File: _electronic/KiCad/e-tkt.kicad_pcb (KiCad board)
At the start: 2 copper layers, 71.1 x 63 mm, 82 parts, among them J2 USB4120-03-C_REVA, Q1 SS8050-G, Q2 SS8050-G, U2 AZ1117I-3.3, U6 ESP32-S3-WROOM-1-N8R2

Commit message: needs revision
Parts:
- removed D2: LED, LED_SMD:LED_0603_1608Metric_Pad1.05x0.95mm_HandSolder
- added D11: LED, LED_SMD:LED_0603_1608Metric_Pad1.05x0.95mm_HandSolder, F.Cu at (140.3, -204.7)
- added R2: 430R, Resistor_SMD:R_0603_1608Metric, F.Cu at (138.7, -207.3)
- added TP_IO15: TestPoint, TestPoint:TestPoint_Pad_D1.0mm, B.Cu at (151.4, -208.8)
- added TP_IO18: TestPoint, TestPoint:TestPoint_Pad_D1.0mm, B.Cu at (151.4, -206.8)
- added TP_IO5: TestPoint, TestPoint:TestPoint_Pad_D1.0mm, B.Cu at (151.4, -214.9)
- added TP_IO6: TestPoint, TestPoint:TestPoint_Pad_D1.0mm, B.Cu at (151.4, -212.9)
- added TP_IO7: TestPoint, TestPoint:TestPoint_Pad_D1.0mm, B.Cu at (151.4, -210.8)
- added TP_IO8: TestPoint, TestPoint:TestPoint_Pad_D1.0mm, B.Cu at (151.4, -204.7)
- moved C11 2.54 mm to (141.7, -207.3)
- moved C10 1.52 mm to (140.2, -207.3)
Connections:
- C11 pad 1: Net-(C11-Pad1) -> +3.3V
- U6 pad 11: unconnected-(U6-Pad11) -> Net-(U6-Pad11)
- U6 pad 12: unconnected-(U6-Pad12) -> Net-(U6-Pad12)
- U6 pad 5: unconnected-(U6-Pad5) -> Net-(U6-Pad5)
- U6 pad 6: unconnected-(U6-Pad6) -> Net-(U6-Pad6)
- U6 pad 7: unconnected-(U6-Pad7) -> Net-(U6-Pad7)
- U6 pad 8: unconnected-(U6-Pad8) -> Net-(U6-Pad8)
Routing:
- net +3.3V: track 266.6 -> 277.8 mm
- net Net-(U6-Pad8): track 0.00 -> 5.06 mm, vias 0 -> 1
- net GNDREF: track 419.0 -> 423.8 mm, vias 11 -> 10
- net Net-(U6-Pad7): track 0.00 -> 4.74 mm, vias 0 -> 1
- net Net-(U6-Pad12): track 0.00 -> 4.34 mm, vias 0 -> 1
- net Net-(U6-Pad11): track 0.00 -> 4.28 mm, vias 0 -> 1
- net Net-(U6-Pad6): track 0.00 -> 4.13 mm, vias 0 -> 1
- net Net-(U6-Pad5): track 0.00 -> 4.09 mm, vias 0 -> 1
- net IO20 D+: track 29.6 -> 31.7 mm
- net Net-(D11-Pad2): track 0.00 -> 2.04 mm
- net Net-(C11-Pad1): track 1.81 -> 0.00 mm
- net +12V: track 188.3 -> 190.1 mm
- net IO19 D-: track 36.0 -> 37.8 mm
- net Net-(J_masterpower1-Pad1): track 23.3 -> 24.9 mm
- net IO16: track 49.1 -> 50.3 mm
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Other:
- board text added: "05"
- board text added: "06"
- board text added: "07"
- board text added: "08"
- board text added: "15"
- board text added: "18"
- board text added: "GPIOs"

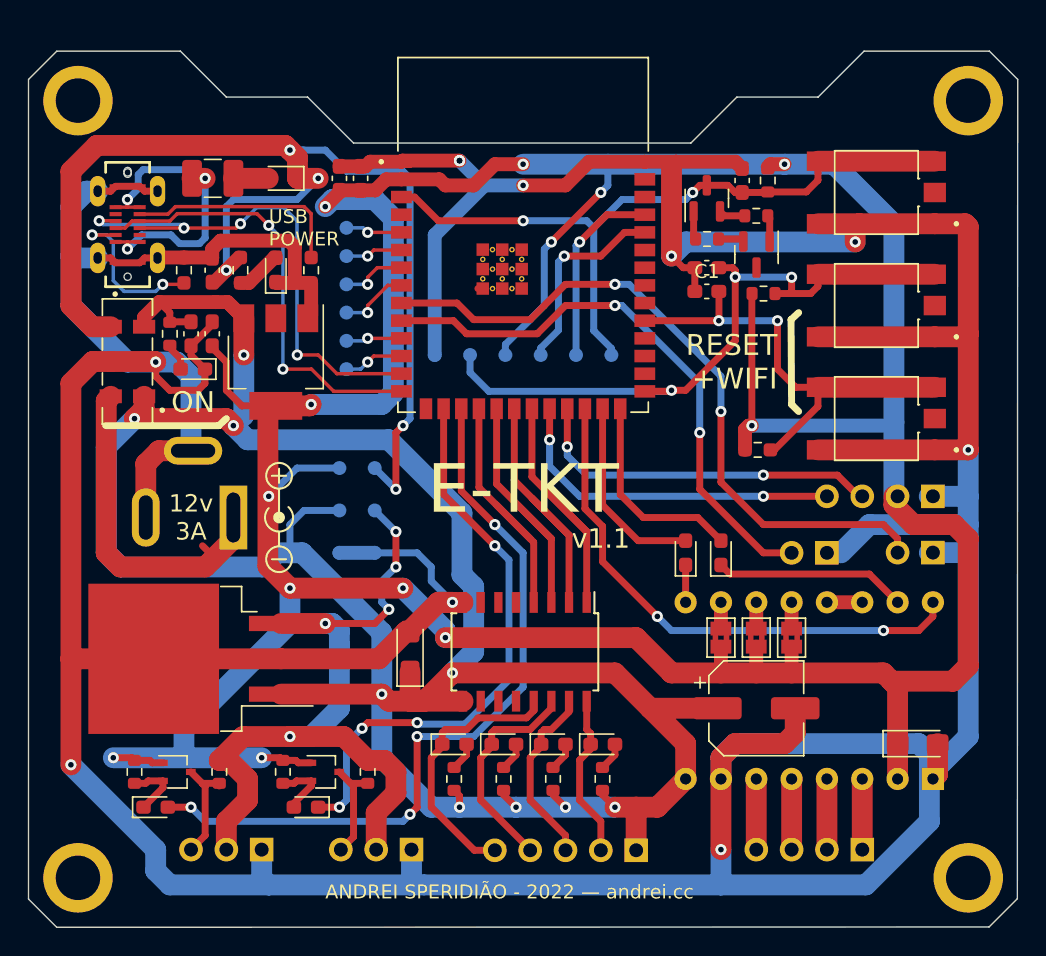
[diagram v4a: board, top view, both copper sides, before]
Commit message: tvs diode, ground plane, schematics layout
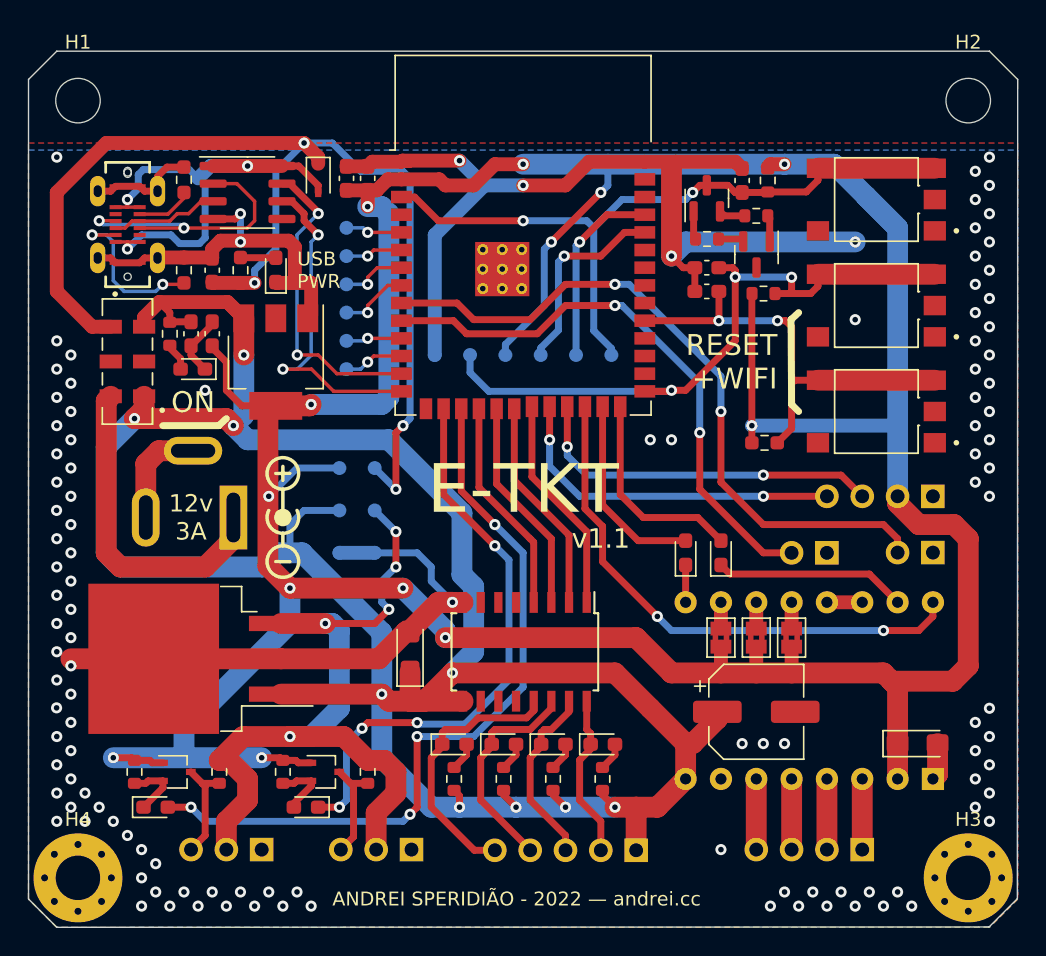
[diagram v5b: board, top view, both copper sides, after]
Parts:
- removed C13: 10uF/25v, Capacitor_SMD:C_0603_1608Metric_Pad1.08x0.95mm_HandSolder
- removed F2: 500mA, Fuse:Fuse_1210_3225Metric_Pad1.42x2.65mm_HandSolder
- removed REF**: Symbol_Barrel_Polarity, Symbol:Symbol_Barrel_Polarity
- removed REF** (x4): MountingHole_3.2mm_M3, MountingHole:MountingHole_3.2mm_M3
- removed REF**: OSHW-Symbol_6.7x6mm_SilkScreen, Symbol:OSHW-Symbol_6.7x6mm_SilkScreen
- added C2: 10uF/25v, Capacitor_SMD:C_0603_1608Metric_Pad1.08x0.95mm_HandSolder, F.Cu at (141.7, -211.8)
- added H1: MountingHole_Pad, MountingHole:MountingHole_3.2mm_M3, F.Cu at (132.1, -224.0)
- added H2: MountingHole_Pad, MountingHole:MountingHole_3.2mm_M3, F.Cu at (196.1, -224.0)
- added H3: MountingHole_Pad, MountingHole:MountingHole_3.2mm_M3_Pad_Via, F.Cu at (196.1, -168.1)
- added H4: MountingHole_Pad, MountingHole:MountingHole_3.2mm_M3_Pad_Via, F.Cu at (132.1, -168.1)
- added U1: USB6B1, Package_SO:SOIC-8_3.9x4.9mm_P1.27mm, F.Cu at (144.3, -217.4)
- U6: footprint SnapEDA Library:XCVR_ESP32-S3-WROOM-1-N16R2 -> RF_Module:ESP32-S3-WROOM-1
- U_6v2: footprint Package_TO_SOT_SMD:TO-263-3_TabPin2 -> Package_TO_SOT_SMD:TO-263-2
- moved R21 11.2 mm to (139.7, -218.3), turned to -90 degrees
- moved D3 2.54 mm to (149.4, -218.4), turned to -90 degrees
- moved R4 0.71 mm to (181.4, -199.4), turned to 180 degrees
- moved S_BOOT1 0.51 mm to (189.5, -216.9)
- moved C6 0.51 mm to (152.9, -218.4)
- moved C7 0.51 mm to (151.4, -218.4)
- moved S_WIFIRESET1 0.51 mm to (189.5, -201.7)
- moved C8 0.25 mm to (180.8, -180.1)
- turned R1 to 90 degrees
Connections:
- D3 pad 2: Net-(D3-Pad2) -> /VBUS_A
- J2 pad A4: Net-(F2-Pad1) -> /VBUS_A
- J2 pad A6: IO20 D+ -> /D1+
- J2 pad A7: IO19 D- -> /D1-
- J2 pad A9: Net-(F2-Pad1) -> /VBUS_A
- J2 pad B4: Net-(F2-Pad1) -> /VBUS_A
- J2 pad B6: IO20 D+ -> /D1+
- J2 pad B7: IO19 D- -> /D1-
- J2 pad B9: Net-(F2-Pad1) -> /VBUS_A
- R6 pad 1: +5V -> Net-(D_USBIN1-Pad2)
- R6 pad 2: Net-(D_USBIN1-Pad2) -> +5V
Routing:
- net GNDREF: track 423.8 -> 159.2 mm, vias 10 -> 117
- net /VBUS_A: track 0.00 -> 35.2 mm, vias 0 -> 3
- net Net-(F2-Pad1): track 23.5 -> 0.00 mm, vias 3 -> 0
- net /D1-: track 0.00 -> 20.9 mm, vias 0 -> 2
- net IO19 D-: track 37.8 -> 22.9 mm, vias 4 -> 2
- net Net-(J2-PadB5): track 15.9 -> 4.07 mm
- net /D1+: track 0.00 -> 7.81 mm
- net IO20 D+: track 31.7 -> 24.4 mm
- net +3.3V: track 277.8 -> 272.9 mm
- net IO13: track 19.3 -> 15.6 mm
- net IO12: track 19.3 -> 15.6 mm
- net IO11: track 19.3 -> 15.6 mm
- net IO10: track 19.0 -> 15.6 mm
- net +5V: track 84.0 -> 81.4 mm, vias 5 -> 4
- net Net-(D3-Pad2): track 2.51 -> 0.00 mm
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- added copper zone on B.Cu, net GNDREF
- added copper zone on F.Cu, net GNDREF
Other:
- outline, holes or cut-outs redrawn
- board text added: "USB PWR"
- board text removed: "USB POWER"

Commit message: fixed esp footprint/symbol, plus vias and holes
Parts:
- removed U6: ESP32-S3-WROOM-1-N8R2, RF_Module:ESP32-S3-WROOM-1
- added U3: ESP32-S3-WROOM-1-N8R2_Andrei, SnapEDA Library:ESP32-S3-WROOM-1_Andrei, F.Cu at (164.1, -214.4)
- H1, H2: footprint MountingHole:MountingHole_3.2mm_M3 -> MountingHole:MountingHole_3.2mm_M3_Pad_Via
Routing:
- net GNDREF: track 159.2 -> 82.4 mm, vias 117 -> 166
- net +5V: track 81.4 -> 62.6 mm, vias 4 -> 5
- net +3.3V: track 272.9 -> 274.5 mm

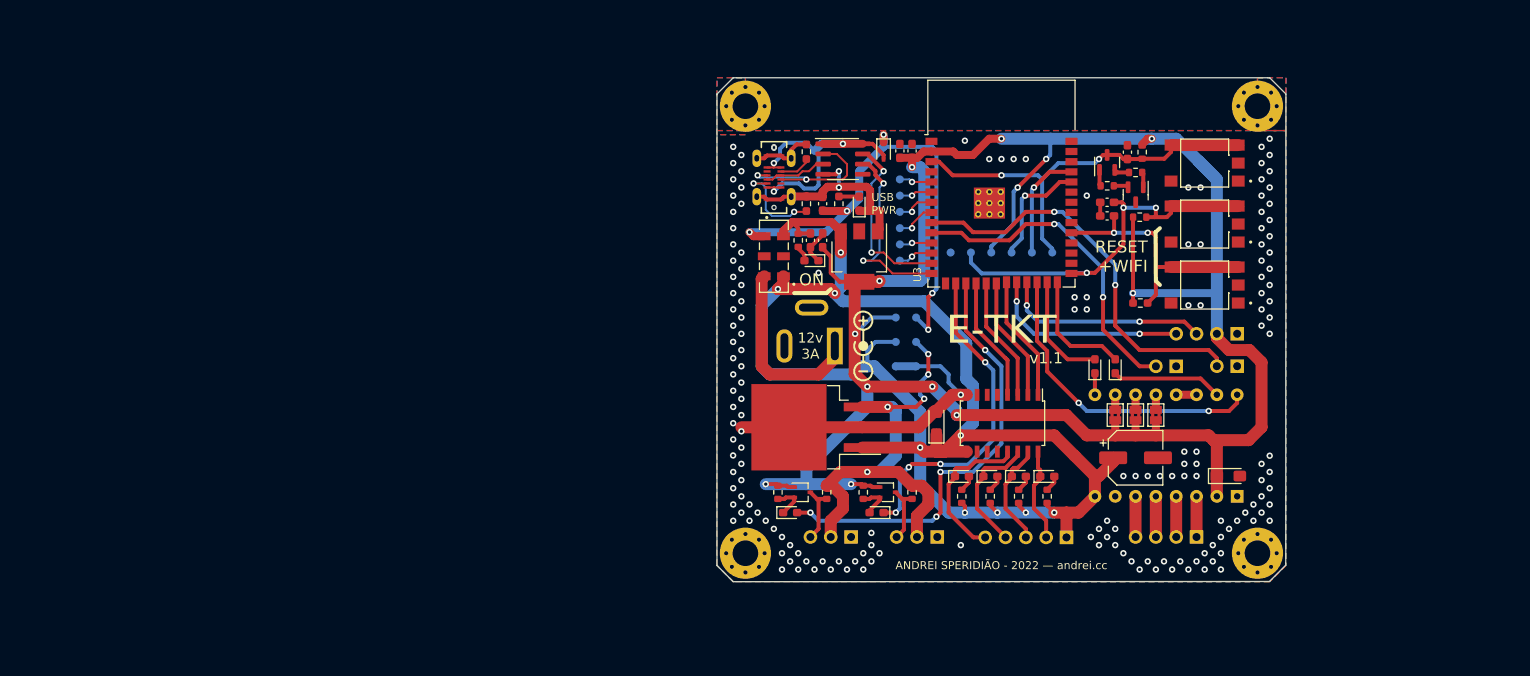
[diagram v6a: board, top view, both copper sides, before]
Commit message: bigger board, switch back to esp32
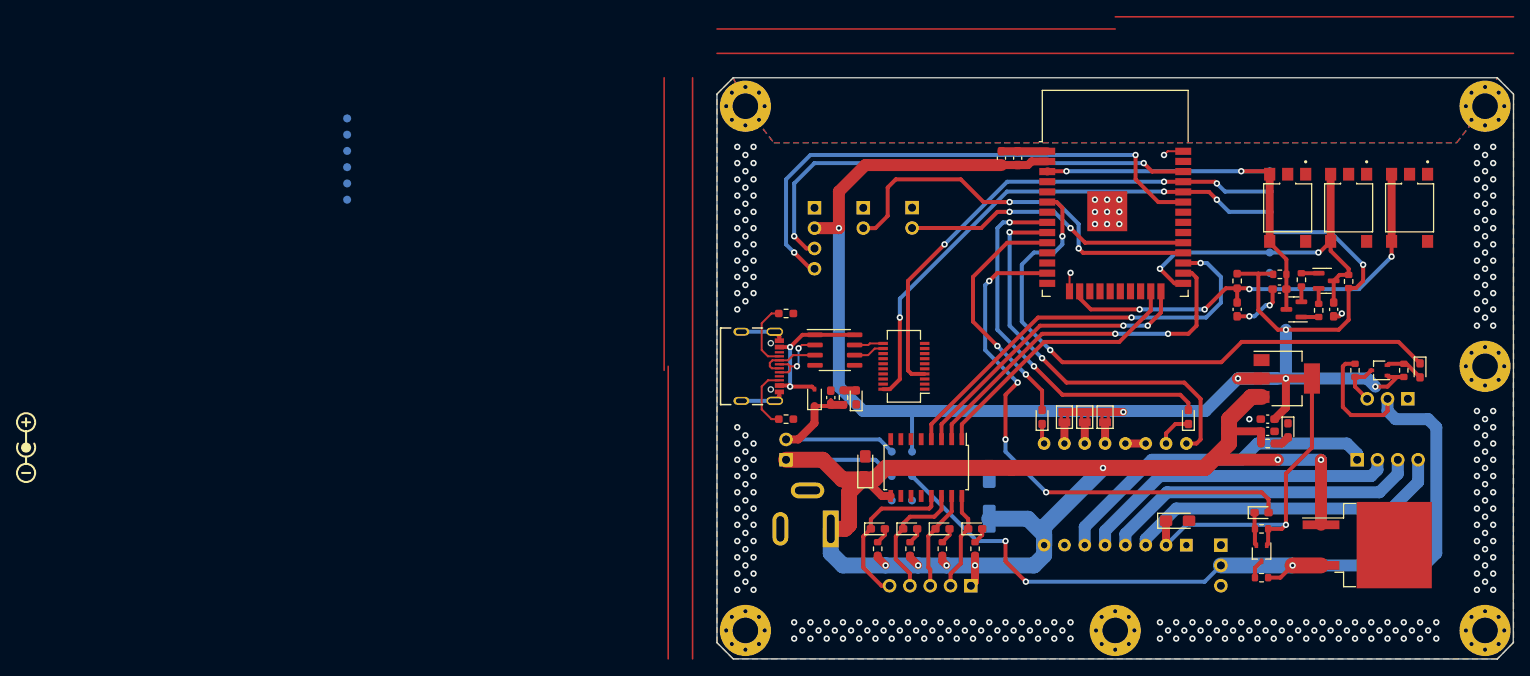
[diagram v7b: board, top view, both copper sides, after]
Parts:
- removed D3: BAT760,115, Diode_SMD:D_SOD-323
- removed J2: USB4120-03-C_REVA, SnapEDA Library:GCT_USB4120-03-C_REVA
- removed R21, R22: 5.1K(10%), Resistor_SMD:R_0603_1608Metric_Pad0.98x0.95mm_HandSolder
- removed S_power1: JS202011JCQN, SnapEDA Library:SW_JS202011JCQN
- added D2: BAT760,115, Diode_SMD:D_SOD-323, F.Cu at (140.7, -187.6)
- added H5: MountingHole_Pad, MountingHole:MountingHole_3.2mm_M3_Pad_Via, F.Cu at (224.5, -191.5)
- added H6: MountingHole_Pad, MountingHole:MountingHole_3.2mm_M3_Pad_Via, F.Cu at (178.3, -158.5)
- added J1: USB4105-GF-A, SnapEDA Library:GCT_USB4105-GF-A, F.Cu at (131.6, -191.5)
- added J_USBPOWER1: Conn_01x02_Male, Connector_PinHeader_2.54mm:PinHeader_1x02_P2.54mm_Vertical, B.Cu at (137.2, -179.8)
- added R3: 5.1K(10%), Resistor_SMD:R_0603_1608Metric_Pad0.98x0.95mm_HandSolder, F.Cu at (137.2, -198.1)
- added R9: 5.1K(10%), Resistor_SMD:R_0603_1608Metric_Pad0.98x0.95mm_HandSolder, F.Cu at (137.2, -184.9)
- added U4: ESP32-WROOM-32, RF_Module:ESP32-WROOM-32, F.Cu at (178.3, -210.1)
- C8: moved to B.Cu
- U3: value ESP32-S3-WROOM-1-N8R2_Andrei -> FT231XS; footprint SnapEDA Library:ESP32-S3-WROOM-1_Andrei -> Package_SO:SSOP-20_3.9x8.7mm_P0.635mm
- moved U_6v2 70.5 mm to (209.8, -169.2), turned to 0 degrees
- moved D9 70.2 mm to (216.4, -191.0), turned to -90 degrees
- moved TP_IO15 69.5 mm to (82.3, -216.4)
- moved TP_IO18 69.5 mm to (82.3, -214.4)
- moved TP_IO5 69.5 mm to (82.3, -222.5)
- moved TP_IO6 69.5 mm to (82.3, -220.5)
- moved TP_IO7 69.5 mm to (82.3, -218.4)
- moved TP_IO8 69.5 mm to (82.3, -212.3)
- moved R11 69.3 mm to (214.4, -191.0), turned to -90 degrees
- moved R2 63.9 mm to (197.4, -181.9), turned to 0 degrees
- moved Q_HALL1 63.3 mm to (211.3, -191.0), turned to 180 degrees
- moved D11 63.2 mm to (199.9, -183.5), turned to -90 degrees
- moved C10 61.9 mm to (197.4, -183.4), turned to 0 degrees
- moved J_HALL1 61.3 mm to (214.9, -187.5)
- moved R13 60.6 mm to (196.6, -171.2), turned to 0 degrees
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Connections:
- net /VBUS_A renamed Net-(D2-Pad2)
- A_DRIVER1 pad 16: IO47 -> IO33
- C1 pad 2: IO38 -> IO13
- D1 pad 2: IO45 -> IO32
- D10 pad 2: IO09 -> IO14
- D4 pad 2: IO48 -> IO25
- D9 pad 1: IO46 -> IO34
- J_17HS4023_1 pad 1: Net-(A_DRIVER1-Pad3) -> Net-(A_DRIVER1-Pad6)
- J_17HS4023_1 pad 2: Net-(A_DRIVER1-Pad4) -> Net-(A_DRIVER1-Pad5)
- J_17HS4023_1 pad 3: Net-(A_DRIVER1-Pad5) -> Net-(A_DRIVER1-Pad4)
- J_17HS4023_1 pad 4: Net-(A_DRIVER1-Pad6) -> Net-(A_DRIVER1-Pad3)
- J_LED_END1 pad 2: IO16 -> IO5
- J_OLED1 pad 3: IO21 -> IO22
- J_OLED1 pad 4: IO14 -> IO21
- J_masterpower1 pad 1: Net-(J_masterpower1-Pad1) -> +12V
- Q2 pad 3: IO0 -> IO0 RESET
- R4 pad 1: IO38 -> IO13
- S_WIFIRESET1 pad 2: IO38 -> IO13
- S_WIFIRESET1 pad 4: IO38 -> IO13
- TP_IO15 pad 1: Net-(TP_IO15-Pad1) -> unconnected-(TP_IO15-Pad1)
- TP_IO18 pad 1: Net-(TP_IO18-Pad1) -> unconnected-(TP_IO18-Pad1)
- TP_IO5 pad 1: Net-(TP_IO5-Pad1) -> unconnected-(TP_IO5-Pad1)
- TP_IO6 pad 1: Net-(TP_IO6-Pad1) -> unconnected-(TP_IO6-Pad1)
- TP_IO7 pad 1: Net-(TP_IO7-Pad1) -> unconnected-(TP_IO7-Pad1)
- TP_IO8 pad 1: Net-(TP_IO8-Pad1) -> unconnected-(TP_IO8-Pad1)
- TP_RX1 pad 1: TXD0 -> TXD0 IO1
- TP_TX1 pad 1: RXD0 -> RXD0 IO3
- U1 pad 2: /D1- -> /D1+
- U1 pad 3: /D1+ -> /D1-
- U1 pad 6: IO20 D+ -> D-
- U1 pad 7: IO19 D- -> D+
- U3 pad 1: GNDREF -> unconnected-(U3-Pad1)
- U3 pad 10: IO17 -> unconnected-(U3-Pad10)
- U3 pad 11: Net-(TP_IO18-Pad1) -> D+
- U3 pad 12: Net-(TP_IO8-Pad1) -> D-
- U3 pad 13: IO19 D- -> unconnected-(U3-Pad13)
- U3 pad 14: IO20 D+ -> unconnected-(U3-Pad14)
- U3 pad 16: IO46 -> unconnected-(U3-Pad16)
- U3 pad 17: IO09 -> unconnected-(U3-Pad17)
- U3 pad 18: IO10 -> unconnected-(U3-Pad18)
- U3 pad 19: IO11 -> unconnected-(U3-Pad19)
- U3 pad 2: +3.3V -> unconnected-(U3-Pad2)
- U3 pad 20: IO12 -> RXD0 IO3
- U3 pad 3: EN -> unconnected-(U3-Pad3)
- U3 pad 4: unconnected-(U3-Pad4) -> TXD0 IO1
- U3 pad 5: Net-(TP_IO5-Pad1) -> unconnected-(U3-Pad5)
- U3 pad 6: Net-(TP_IO6-Pad1) -> GNDREF
- U3 pad 7: Net-(TP_IO7-Pad1) -> unconnected-(U3-Pad7)
- U3 pad 8: Net-(TP_IO15-Pad1) -> unconnected-(U3-Pad8)
- U3 pad 9: IO16 -> unconnected-(U3-Pad9)
- U_DRIVER1 pad 1: IO13 -> IO15
- U_DRIVER1 pad 2: IO12 -> IO4
- U_DRIVER1 pad 3: IO11 -> IO2
- U_DRIVER1 pad 4: IO10 -> IO16
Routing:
- net IO34: track 0.00 -> 74.1 mm, vias 0 -> 2
- net RXD0 IO3: track 0.00 -> 65.5 mm, vias 0 -> 3
- net TXD0 IO1: track 0.00 -> 64.3 mm, vias 0 -> 3
- net +6V: track 56.7 -> 119.9 mm, vias 5 -> 3
- net IO22: track 0.00 -> 59.9 mm, vias 0 -> 2
- net IO09: track 54.8 -> 0.00 mm, vias 4 -> 0
- net GNDREF: track 82.4 -> 29.7 mm, vias 166 -> 253
- net IO33: track 0.00 -> 51.1 mm, vias 0 -> 2
- net IO32: track 0.00 -> 47.8 mm, vias 0 -> 2
- net IO4: track 0.00 -> 45.5 mm, vias 0 -> 2
- net IO14: track 25.0 -> 68.5 mm, vias 2 -> 4
- net IO21: track 25.8 -> 68.1 mm
- net IO46: track 41.4 -> 0.00 mm, vias 4 -> 0
- net IO13: track 15.6 -> 55.3 mm, vias 0 -> 4
- net IO47: track 38.8 -> 0.00 mm, vias 2 -> 0
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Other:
- board size 71.1 x 63 mm -> 99.6 x 72.7 mm
- board text added: "2022/07/07"
- board text added: "USB MODE"
- board text added: "v0.9"
- board text removed: "12v 3A"
- board text removed: "ANDREI SPERIDIÃO - 2022 — andrei.cc"
- board text removed: "E-TKT"
- board text removed: "EXTERNAL FLASHING"
- board text removed: "ON"
- board text removed: "RESET +WIFI"
- board text removed: "USB PWR"
- board text removed: "v1.1"
